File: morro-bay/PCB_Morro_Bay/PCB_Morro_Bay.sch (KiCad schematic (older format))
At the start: 40 parts, among them J1 USB_B, J2 Conn_01x02, U1 MCP2515-xSO, U2 SN65HVD232, U3 MIC5504-3.3YM5, U4 ATSAMD21J18A-AU, Y1 Crystal, Y2 Crystal, Y3 Crystal

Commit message: Add input connectors, DIP switches
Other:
- note added: "Should this be a USB plug? I like it,\nbut could also make it a Microfit."
- note added: "TODO:\n-CRYSTALS\n-CAN CONTROLS\n-LEDS\n-CHECK INPUT CURRENT ON ADC PINS\n-EXTERNAL ADC\n-SERIAL"
- note removed: "TODO:\nGLOBAL LABELS ON INPUTS\nCONNECTORS\nCRYSTALS\nCAN CONTROLS\nLEDS\nDIP SWITCHES\nEXTERNAL ADC"
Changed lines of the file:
@@
 $Descr A4 11693 8268
 encoding utf-8
-Sheet 1 2
+Sheet 1 3
 Title "Morro Bay Data Acquisition Board"
 Date ""
@@
 	9550 1050 9550 1100
 Wire Wire Line
-	9400 1050 9400 1100
+	9400 1000 9400 1100
 Wire Wire Line
 	9550 1050 9650 1050
@@
 L power:+3.3VA #PWR030
 U 1 1 5E4084FC
-P 9400 1050
-F 0 "#PWR030" H 9400 900 50  0001 C CNN
-F 1 "+3.3VA" H 9415 1223 50  0000 C CNN
-F 2 "" H 9400 1050 50  0001 C CNN
-F 3 "" H 9400 1050 50  0001 C CNN
-	1    9400 1050
+P 9400 1000
+F 0 "#PWR030" H 9400 850 50  0001 C CNN
+F 1 "+3.3VA" H 9415 1173 50  0000 C CNN
+F 2 "" H 9400 1000 50  0001 C CNN
+F 3 "" H 9400 1000 50  0001 C CNN
+	1    9400 1000
 	1    0    0    -1
 $EndComp
@@
 	9400 4350 9550 4350
 $Sheet
-S 1100 6000 1650 700
+S 650  6850 1650 700
 U 5E59A680
 F0 "AnalogInput" 50
 F1 "AnalogInput.sch" 50
 $EndSheet
-Text Notes 1350 6450 0    118  ~ 0
+Text Notes 900  7300 0    118  ~ 0
 Analog Input
 Text GLabel 8850 2850 0    50   Input ~ 0
@@
 Wire Wire Line
 	8050 1650 8050 1700
-Text Notes 3900 6950 0    118  ~ 0
-TODO:\nGLOBAL LABELS ON INPUTS\nCONNECTORS\nCRYSTALS\nCAN CONTROLS\nLEDS\nDIP SWITCHES\nEXTERNAL ADC
+Text Notes 3350 6200 0    118  ~ 0
+TODO:\n-CRYSTALS\n-CAN CONTROLS\n-LEDS\n-CHECK INPUT CURRENT ON ADC PINS\n-EXTERNAL ADC\n-SERIAL
+Text Notes 500  2250 0    50   ~ 0
+Should this be a USB plug? I like it,\nbut could also make it a Microfit.
 $EndSCHEMATC

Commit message: Switch to DC-DC reg
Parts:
- removed J1: USB_B, symbol Connector:USB_B
- added C?: 10uF, symbol Device:C
- added C?: 22uF, symbol Device:C
- added D? (x2): LED, symbol Device:LED
- added J?: Conn_01x02, symbol Connector_Generic:Conn_01x02
- added R?: 300, symbol Device:R_US
- added R?: 130, symbol Device:R_US
- added U?: V7805-2000R, symbol Morro_Bay_Lib:V7805-2000R
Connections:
- wire segments 183 -> 199
- no-connect marks 2 -> 0
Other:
- note added: "TODO:\n-CRYSTALS\n-CAN CONTROLS\n-LEDS\n-EXTERNAL ADC\n-SERIAL\n-PROGRAMMING HEADER"
- note removed: "Should this be a USB plug? I like it,\nbut could also make it a Microfit."
- note removed: "TODO:\n-CRYSTALS\n-CAN CONTROLS\n-LEDS\n-CHECK INPUT CURRENT ON ADC PINS\n-EXTERNAL ADC\n-SERIAL"
- moved on the sheet: C3, C4, C5, C7, C8, FB1, U3

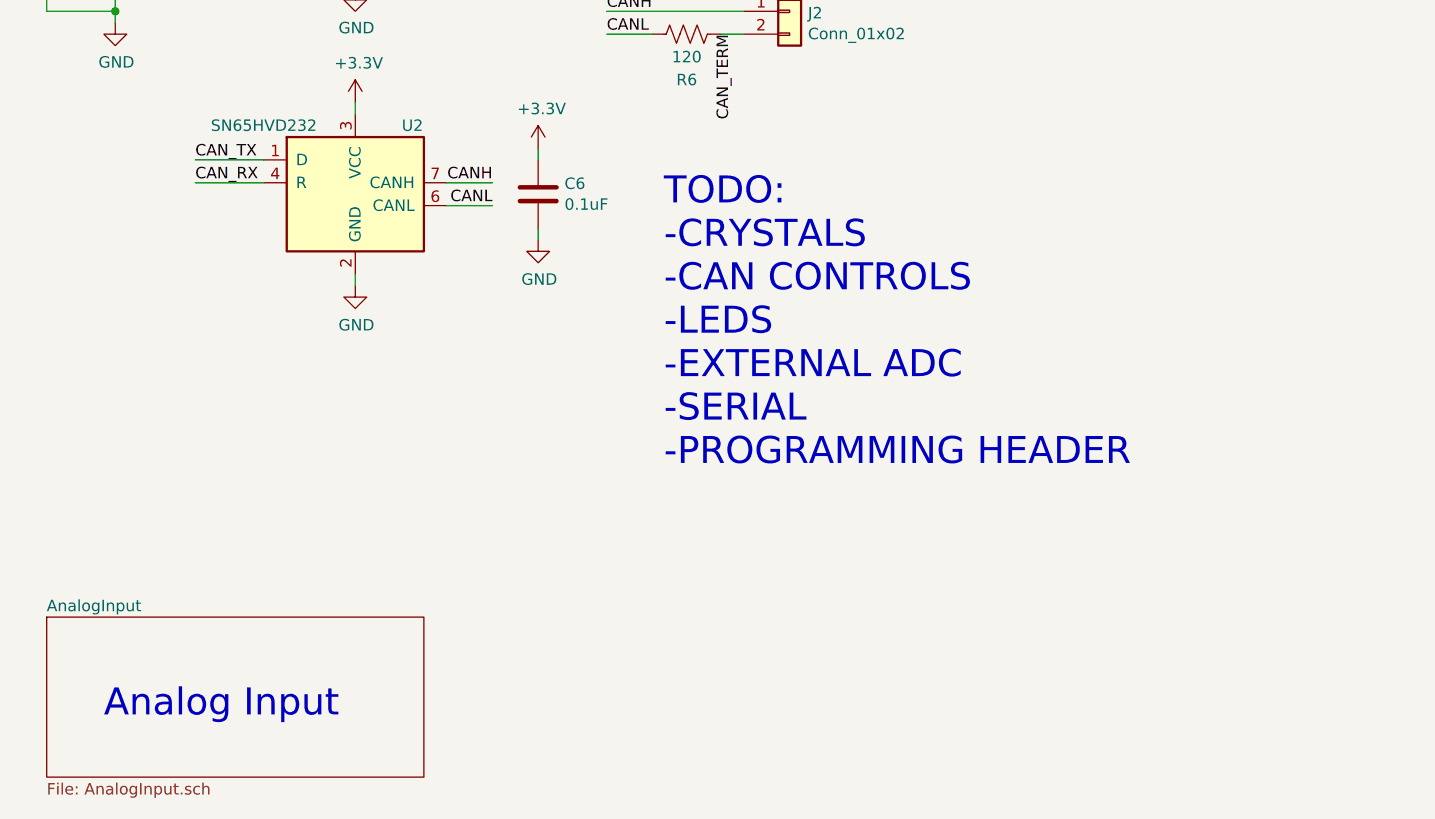
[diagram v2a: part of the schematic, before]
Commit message: Add external ADC
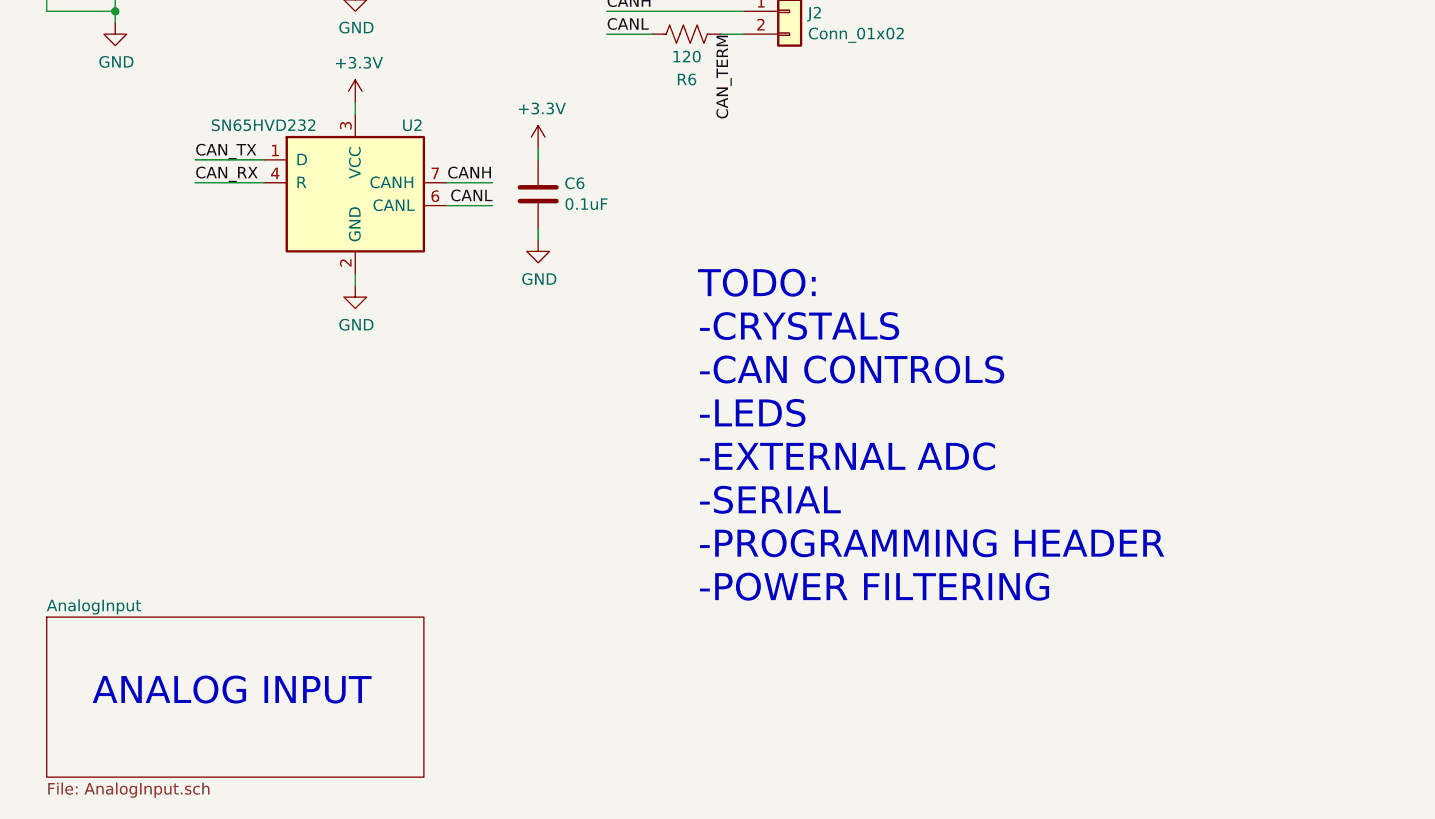
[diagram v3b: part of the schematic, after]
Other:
- note added: "ANALOG INPUT"
- note added: "TODO:\n-CRYSTALS\n-CAN CONTROLS\n-LEDS\n-EXTERNAL ADC\n-SERIAL\n-PROGRAMMING HEADER\n-POWER FILTERING"
- note removed: "Analog Input"
- note removed: "TODO:\n-CRYSTALS\n-CAN CONTROLS\n-LEDS\n-EXTERNAL ADC\n-SERIAL\n-PROGRAMMING HEADER"
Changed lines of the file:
@@
 $Descr A4 11693 8268
 encoding utf-8
-Sheet 1 3
+Sheet 1 4
 Title "Morro Bay Data Acquisition Board"
 Date ""
@@
 F1 "AnalogInput.sch" 50
 $EndSheet
-Text Notes 900  7300 0    118  ~ 0
-Analog Input
+Text Notes 850  7250 0    118  ~ 0
+ANALOG INPUT
 Text GLabel 8850 2850 0    50   Input ~ 0
 SAMD_ADC_1
@@
 Wire Wire Line
 	8050 1650 8050 1700
-Text Notes 3350 6200 0    118  ~ 0
-TODO:\n-CRYSTALS\n-CAN CONTROLS\n-LEDS\n-EXTERNAL ADC\n-SERIAL\n-PROGRAMMING HEADER
+Text Notes 3500 6800 0    118  ~ 0
+TODO:\n-CRYSTALS\n-CAN CONTROLS\n-LEDS\n-EXTERNAL ADC\n-SERIAL\n-PROGRAMMING HEADER\n-POWER FILTERING
 $Comp
 L Device:LED D?

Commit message: External ADC, SPI
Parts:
- removed J2: Conn_01x02, symbol Connector_Generic:Conn_01x02
- removed L1: L, symbol Device:L
- added C29: 0.1uF, symbol Device:C
- added FB2: Ferrite_Bead, symbol Device:Ferrite_Bead
- added J2: Conn_01x04, symbol Connector_Generic:Conn_01x04
- added J23: Conn_02x03, symbol Connector_Generic:Conn_02x03_Counter_Clockwise
- added JP1: Jumper_NC_Small, symbol Device:Jumper_NC_Small
- added R71: 330, symbol Device:R_US
- added R72: 10K, symbol Device:R_US
- added R73: 1K, symbol Device:R_US
- added SW3: SW_Push, symbol Switch:SW_Push
- FB1: value Ferrite_Bead -> HI2220P701R-10; Digikey (none) -> 240-2428-1-ND
- gave numbers to parts that had none: 8
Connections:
- net labels added: EADC_CS, EADC_DIN, EADC_DOUT_DRDY, EADC_RESET, EADC_SCLK, EADC_START_SYNC, GPIO_1, GPIO_2, GPIO_3, GPIO_4, LED_1, LED_2, SAMD_nRESET, SWCLK, SWDIO
- wire segments 199 -> 253
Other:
- note added: "700 ohms @ 100MHz"
- note added: "TODO:\n-CRYSTALS\n-LEDS\n-POWER FILTERING"
- note removed: "TODO:\n-CRYSTALS\n-CAN CONTROLS\n-LEDS\n-EXTERNAL ADC\n-SERIAL\n-PROGRAMMING HEADER\n-POWER FILTERING"
- moved on the sheet: C10, C11, C12, C13, C14, C15, C16, C17, C18, C19, C20, C21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

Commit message: Ready for initial sch review
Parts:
- added D? (x2): LED, symbol Device:LED
- added J? (x2): Conn_01x04, symbol Connector_Generic:Conn_01x04
- added R? (x2): 130, symbol Device:R_US
- C1, C2: value C -> 22pF
- FB2: value Ferrite_Bead -> FBMH3216HM221NTV; Digikey (none) -> 587-3834-1-ND
- Y1: value Crystal -> 8MHz
- Y2: value Crystal -> 30MHz
- Y3: value Crystal -> 32.768kHz
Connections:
- net +3V3: now also J?.3 (Pin_3)
- net +5V: now also J?.4 (Pin_4)
- net GND: now also J?.1 (Pin_1), J?.2 (Pin_2), R?.2, R?.2
- net GPIO_1: now also J?.1 (Pin_1)
- net GPIO_2: now also J?.2 (Pin_2)
- net GPIO_3: now also J?.3 (Pin_3)
- net GPIO_4: now also J?.4 (Pin_4)
- net LED_1: now also D?.2 (A)
- net LED_2: now also D?.2 (A)
- new net: D?.1 (K), R?.1 (x2)
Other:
- note removed: "TODO:\n-CRYSTALS\n-LEDS\n-POWER FILTERING"
- moved on the sheet: J23

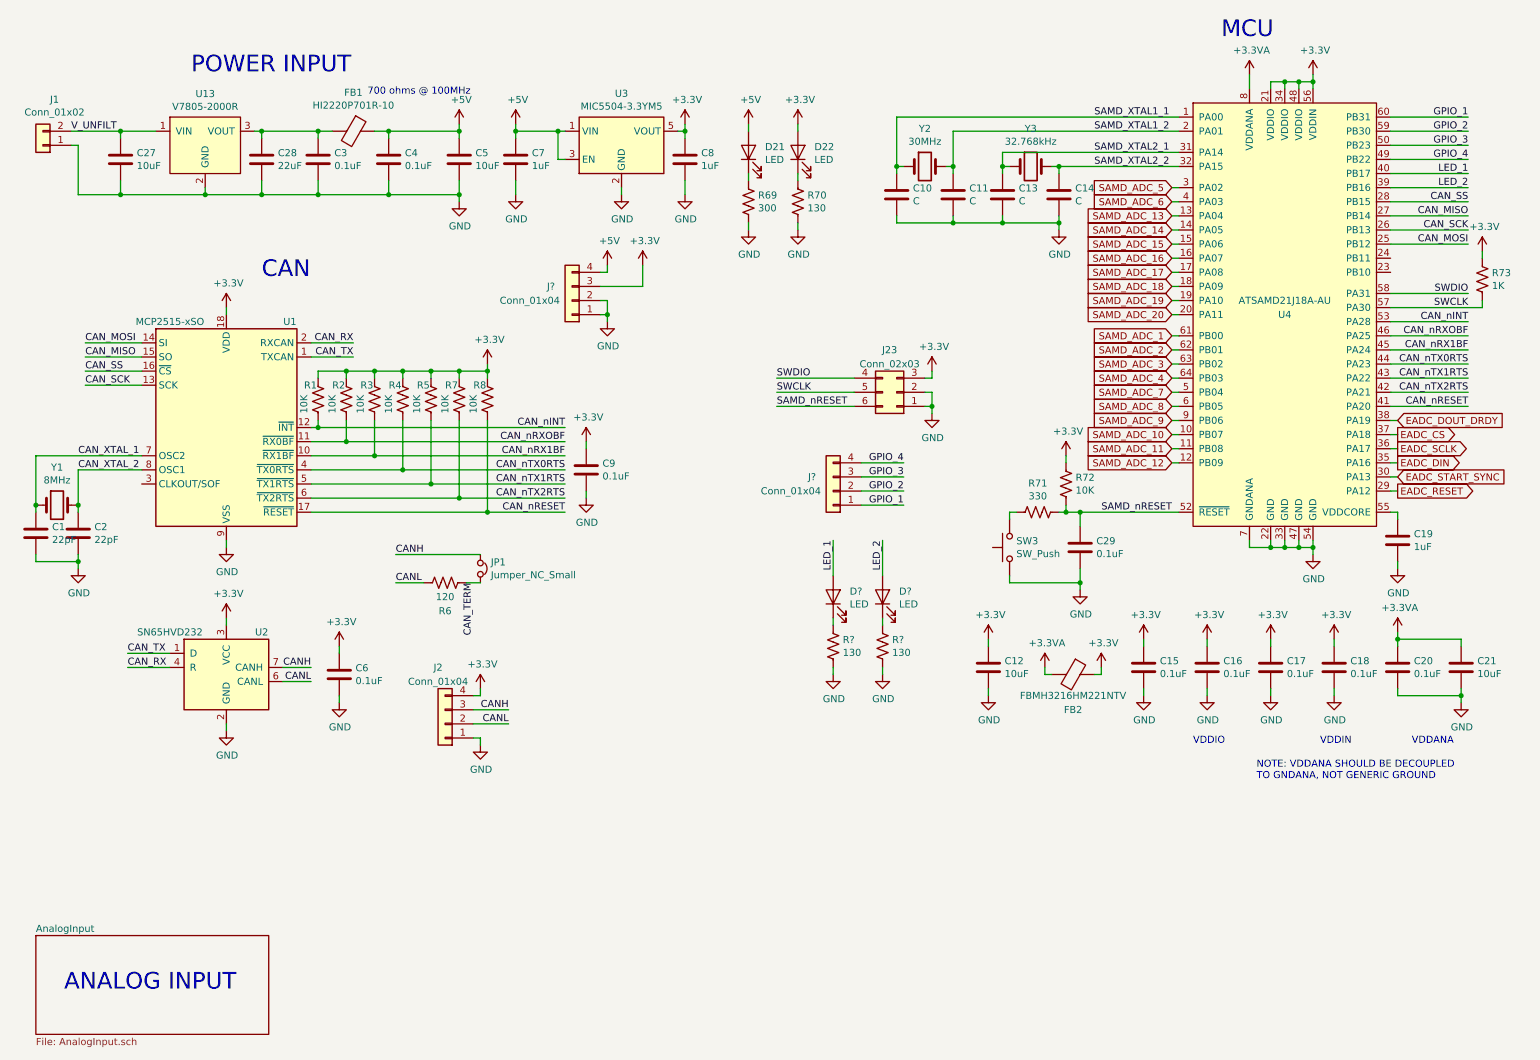
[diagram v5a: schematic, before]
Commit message: Work on BOM
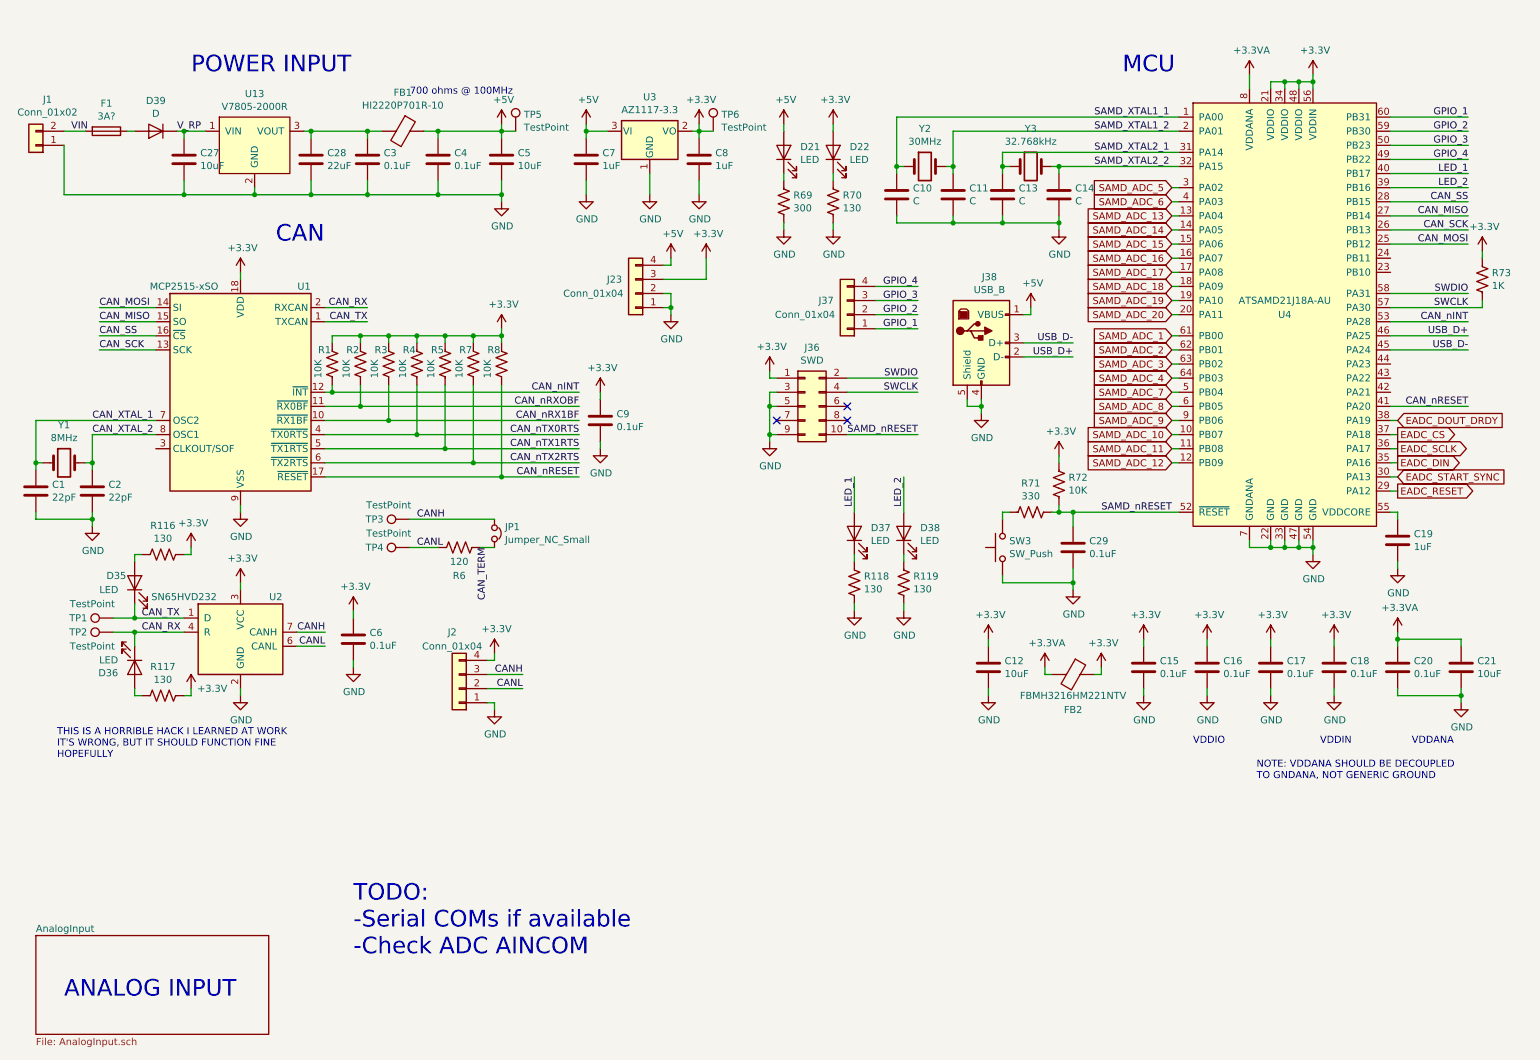
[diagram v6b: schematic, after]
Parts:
- removed J23: Conn_02x03, symbol Connector_Generic:Conn_02x03_Counter_Clockwise
- removed U3: MIC5504-3.3YM5, Package_TO_SOT_SMD:SOT-23-5, symbol Regulator_Linear:MIC5504-3.3YM5
- added D35, D36: LED, symbol Device:LED
- added D39: D, symbol Device:D
- added F1: 3A?, symbol Device:Fuse
- added J36: SWD, symbol Connector_Generic:Conn_02x05_Odd_Even
- added J38: USB_B, symbol Connector:USB_B
- added R116, R117: 130, symbol Device:R_US
- added TP1, TP2, TP3, TP4, TP5, TP6: TestPoint, symbol Connector:TestPoint
- added U3: AZ1117-3.3, symbol Regulator_Linear:AZ1117-3.3
- C15, C16, C17, C18, C20, C3, C4, C6, C9: footprint (none) -> Capacitor_SMD:C_0603_1608Metric_Pad1.05x0.95mm_HandSolder; Digikey (none) -> https://www.digikey.ca/product-detail/en/yageo/CC0603KRX7R8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; Part Number (none) -> CC0603KRX7R8BB104
- FB2: footprint (none) -> Inductor_SMD:L_1206_3216Metric_Pad1.42x1.75mm_HandSolder; Digikey 587-3834-1-ND -> https://www.digikey.ca/products/en?keywords=587-3834-1-ND; Part Number (none) -> FBMH3216HM221NTV
- gave numbers to parts that had none: 6
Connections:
- net +3V3: now also J36.1 (Pin_1), R116.1, R117.1, TP6.1, U3.2 (VO)
- net +5V: now also J38.1 (VBUS), TP5.1, U3.3 (VI)
- net CANH: now also TP3.1
- net CANL: now also TP4.1
- net CAN_RX: now also D36.1 (K), TP2.1
- net CAN_TX: now also D35.1 (K), TP1.1
- net CAN_nRX1BF: no longer U4.45 (PA24)
- net CAN_nRXOBF: no longer U4.46 (PA25)
- net CAN_nTX0RTS: no longer U4.44 (PA23)
- net CAN_nTX1RTS: no longer U4.43 (PA22)
- net CAN_nTX2RTS: no longer U4.42 (PA21)
- net GND: now also J36.3 (Pin_3), J36.5 (Pin_5), J36.9 (Pin_9), J38.4 (GND), J38.5 (Shield), U3.1 (GND)
- net SAMD_nRESET: now also J36.10 (Pin_10)
- net SWCLK: now also J36.4 (Pin_4)
- net SWDIO: now also J36.2 (Pin_2)
- net V_UNFILT renamed V_RP
- net V_RP: now also D39.1 (K); no longer J1.2 (Pin_2)
- new net: D39.2 (A), F1.1
- new net: D36.2 (A), R117.2
- new net: D35.2 (A), R116.2
- new net USB_D+: J38.2 (D-), U4.46 (PA25)
- new net USB_D-: J38.3 (D+), U4.45 (PA24)
- new net VIN: F1.2, J1.2 (Pin_2)
- no-connect marks 0 -> 3
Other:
- note added: "THIS IS A HORRIBLE HACK I LEARNED AT WORK\nIT'S WRONG, BUT IT SHOULD FUNCTION FINE\nHOPEFULLY"
- note added: "TODO:\n-Serial COMs if available\n-Check ADC AINCOM"
- moved on the sheet: C1, C2, C27, C28, C29, C5, C7, C8, D21, D22, D37, D38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

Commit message: More BOM
And if that don't work, use more gun.
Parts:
- C12, C21, C5: footprint (none) -> Capacitor_SMD:C_0603_1608Metric_Pad1.05x0.95mm_HandSolder; Digikey (none) -> https://www.digikey.ca/en/products/detail/samsung-electro-m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; Part Number (none) -> CL10A106MA8NRNC
- C19, C7, C8: footprint (none) -> Capacitor_SMD:C_0603_1608Metric_Pad1.05x0.95mm_HandSolder; Digikey (none) -> https://www.digikey.ca/en/products/detail/samsung-electro-m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; Part Number (none) -> CL10B105KA8NNNC
- C27: footprint (none) -> Capacitor_SMD:C_1210_3225Metric_Pad1.42x2.65mm_HandSolder; Digikey (none) -> https://www.digikey.ca/en/products/detail/murata-electronic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; Part Number (none) -> GRM32EC72A106KE05L
- C28: footprint (none) -> Capacitor_SMD:C_0805_2012Metric_Pad1.15x1.40mm_HandSolder; Digikey (none) -> https://www.digikey.ca/product-detail/en/samsung-electro-me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; Part Number (none) -> CL21A226MAQNNNE
- C29: footprint (none) -> Capacitor_SMD:C_0603_1608Metric_Pad1.05x0.95mm_HandSolder; Digikey (none) -> https://www.digikey.ca/product-detail/en/yageo/CC0603KRX7R8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; Part Number (none) -> CC0603KRX7R8BB104
- D39: value D -> STPS5L60S; footprint (none) -> Diode_SMD:D_SMC_Handsoldering; Digikey (none) -> https://www.digikey.ca/product-detail/en/stmicroelectronics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; Part Number (none) -> STPS5L60S
- F1: value 3A? -> 3A; Digikey (none) -> https://www.digikey.ca/product-detail/en/littelfuse-inc/015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; Part Number (none) -> 0154003.DR
- R116, R117: value 130 -> 500
- R118, R119, R70: value 130 -> 330
- R69: value 300 -> 600
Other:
- note added: "TODO:\n-Serial COMs if available\n-Check ADC AINCOM\n-INAMPs"
- note removed: "TODO:\n-Serial COMs if available\n-Check ADC AINCOM"
- moved on the sheet: C27

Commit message: More bom
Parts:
- removed J37: Conn_01x04, symbol Connector_Generic:Conn_01x04
- added J37, J39: Conn_01x06, symbol Connector_Generic:Conn_01x06
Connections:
- net +5V: now also J37.6 (Pin_6), J39.6 (Pin_6)
- net GND: now also J37.1 (Pin_1), J39.1 (Pin_1)
- net GPIO_1: now also U4.44 (PA23), J37.2 (Pin_2); no longer U4.60 (PB31)
- net GPIO_2: now also U4.43 (PA22), J37.3 (Pin_3); no longer U4.59 (PB30)
- net GPIO_3: now also U4.42 (PA21), J37.4 (Pin_4); no longer U4.50 (PB23)
- net GPIO_4: now also U4.24 (PB11), J37.5 (Pin_5); no longer U4.49 (PB22)
- net LED_1: now also U4.39 (PB16); no longer U4.40 (PB17)
- net LED_2: now also U4.40 (PB17); no longer U4.39 (PB16)
- new net ESERCOM_0: J39.2 (Pin_2), U4.59 (PB30)
- new net ESERCOM_1: J39.3 (Pin_3), U4.60 (PB31)
- new net ESERCOM_2: J39.4 (Pin_4), U4.49 (PB22)
- new net ESERCOM_3: J39.5 (Pin_5), U4.50 (PB23)
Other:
- note added: "TODO:\n-Check ADC AINCOM\n-INAMPs"
- note removed: "TODO:\n-Serial COMs if available\n-Check ADC AINCOM\n-INAMPs"
- moved on the sheet: D37, D38, J36, R118, R119
